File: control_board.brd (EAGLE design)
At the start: 90.2 x 72.3 mm, 19 parts

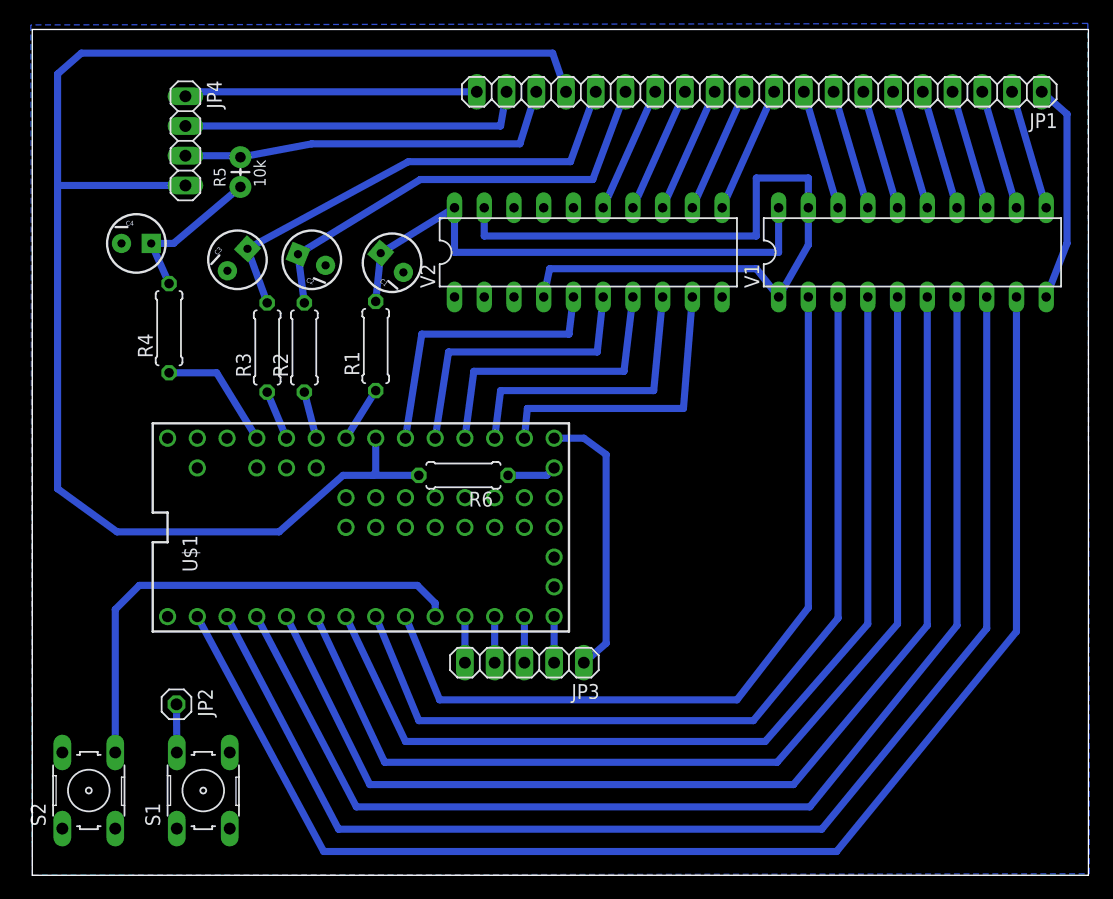
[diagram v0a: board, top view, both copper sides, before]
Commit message: schematic update
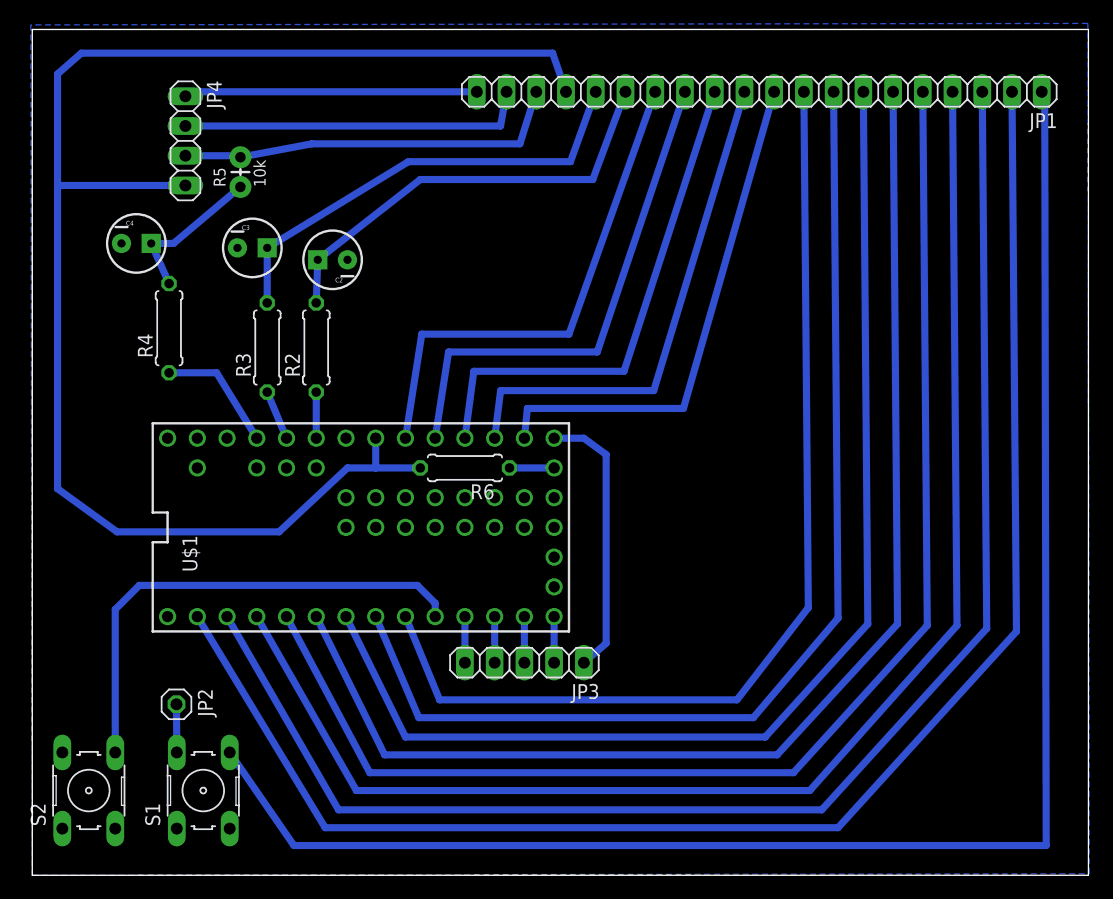
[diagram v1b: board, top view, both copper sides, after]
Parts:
- removed C1: (no value), SparkFun-Capacitors:CPOL-RADIAL-10UF-25V
- removed R1: 330, resistor:0207/7
- removed V1, V2: 74540N, 74ttl-din:DIL20
- moved C2 1.78 mm to (25.7, 52.6), turned to 180 degrees
- moved C3 1.63 mm to (18.8, 53.6), turned to 0 degrees
- moved R2 1.02 mm to (24.3, 45.1)
- moved R6 0.65 mm to (37.0, 34.8)
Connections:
- removed net +UB: C1.1, R1.2, V1.20, V2.20
- removed net N$1: JP1.2, V1.11
- removed net N$10: JP1.12, V2.13
- removed net N$11: JP1.13, V2.14
- removed net N$12: JP1.14, V2.15
- removed net N$13: JP1.10, V2.11
- removed net N$2: JP1.3, V1.12
- removed net N$3: JP1.4, V1.13
- removed net N$4: JP1.5, V1.14
- removed net N$5: JP1.6, V1.15
- removed net N$6: JP1.7, V1.16
- removed net N$7: JP1.8, V1.17
- removed net N$8: JP1.9, V1.18
- removed net N$9: JP1.11, V2.12
- net GND: no longer C1.2, V1.1, V1.10, V1.19, V2.1, V2.10, V2.19, V2.2, V2.3, V2.4
- net LEVEL_SHIFTER_POWER_PIN: no longer R1.1
- net N$15: now also JP1.10; no longer V2.9
- net N$16: now also JP1.11; no longer V2.8
- net N$17: now also JP1.12; no longer V2.7
- net N$18: now also JP1.13; no longer V2.6
- net N$19: now also JP1.2; no longer V1.9
- net N$20: now also JP1.3; no longer V1.8
- net N$21: now also JP1.4; no longer V1.7
- net N$22: now also JP1.5; no longer V1.6
- net N$23: now also JP1.6; no longer V1.5
- net N$24: now also JP1.7; no longer V1.4
- net N$25: now also JP1.8; no longer V1.3
- net N$26: now also JP1.9; no longer V1.2
- net N$28: now also JP1.14; no longer V2.5
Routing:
- net GND: track 87.9 -> 138.6 mm
- net +UB: track 46.9 -> 0.00 mm
- net N$28: track 24.8 -> 43.5 mm
- net N$18: track 24.9 -> 43.6 mm
- net N$17: track 25.0 -> 43.7 mm
- net N$16: track 25.2 -> 43.9 mm
- net N$15: track 25.4 -> 44.0 mm
- net N$26: track 69.6 -> 87.1 mm
- net N$25: track 77.0 -> 94.1 mm
- net N$24: track 83.8 -> 100.7 mm
- net N$23: track 90.9 -> 107.4 mm
- net N$22: track 98.0 -> 113.9 mm
- net N$21: track 105.1 -> 120.3 mm
- net N$20: track 112.3 -> 127.1 mm
- net N$19: track 119.5 -> 133.7 mm
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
